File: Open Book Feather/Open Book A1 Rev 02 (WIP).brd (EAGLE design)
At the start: 77.5 x 112.3 mm, 124 parts, among them J1 SJ-43514-SMT, J2 10118193-0001LF, Q1 DMG341, Q2 IRLML0100, SW1 SPDT_SWITCH, U1 AP2112-3.3, U2 MCP73831T-2ACI/OT, U3 ATSAMD51J64-TQFP(10X10), U4 GD25Q16C (or GD25Q32C), U5 74AC165D, U6 GD25Q16C (or GD25Q32C), U7 23K256-I/SN, U8 MAX4466EXK+T, X1 JSTPH, X2 2x5 0.05" SWD

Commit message: correct component values
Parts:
- L1: value 68uH -> 10uH
- R4, R6: value 270 -> 1K
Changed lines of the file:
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@@
 <attribute name="VALUE" x="3.302" y="102.616" size="0.508" layer="28" font="vector" ratio="18" rot="MR90" align="center"/>
 </element>
-<element name="L1" library="microbuilder" package="INDUCTOR_4X4MM_NR401" value="68uH" x="6.35" y="94.742" smashed="yes" rot="MR270">
+<element name="L1" library="microbuilder" package="INDUCTOR_4X4MM_NR401" value="10uH" x="6.35" y="94.742" smashed="yes" rot="MR270">
 <attribute name="NAME" x="6.382" y="97.114" size="0.508" layer="26" font="vector" ratio="18" rot="MR180" align="center"/>
 <attribute name="VALUE" x="5.366" y="94.844" size="0.508" layer="28" font="vector" ratio="18" rot="MR180" align="center"/>
@@
 <attribute name="VALUE" x="18.088" y="111.887" size="0.508" layer="28" font="vector" ratio="18" rot="MR0" align="center"/>
 </element>
-<element name="R4" library="microbuilder" package="0805-NO" value="270" x="32.2834" y="108.5088" smashed="yes" rot="MR180">
+<element name="R4" library="microbuilder" package="0805-NO" value="1K" x="32.2834" y="108.5088" smashed="yes" rot="MR180">
 <attribute name="NAME" x="32.2834" y="107.315" size="0.508" layer="26" font="vector" ratio="18" rot="MR0" align="center"/>
 <attribute name="VALUE" x="32.2834" y="107.2388" size="0.508" layer="28" font="vector" ratio="18" rot="MR180" align="center"/>
@@
 <attribute name="VALUE" x="26.162" y="37.846" size="0.508" layer="28" font="vector" ratio="18" rot="MR0" align="center"/>
 </element>
-<element name="R6" library="microbuilder" package="0805-NO" value="270" x="45.466" y="108.7882" smashed="yes" rot="MR180">
+<element name="R6" library="microbuilder" package="0805-NO" value="1K" x="45.466" y="108.7882" smashed="yes" rot="MR180">
 <attribute name="NAME" x="47.4472" y="108.458" size="0.508" layer="26" font="vector" ratio="18" rot="MR90" align="center"/>
 <attribute name="VALUE" x="47.0662" y="109.9312" size="0.508" layer="28" font="vector" ratio="18" rot="MR180" align="center"/>

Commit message: remove wire stub
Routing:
- net N$65: track 4.96 -> 4.45 mm
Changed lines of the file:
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@@
 <contactref element="R19" pad="2"/>
 <contactref element="R20" pad="1"/>
-<wire x1="65.344" y1="1.524" x2="65.852" y2="1.524" width="0.1524" layer="16"/>
 <wire x1="65.852" y1="1.524" x2="64.676" y2="2.7" width="0.1524" layer="16"/>
 <wire x1="64.676" y1="2.7" x2="64.008" y2="3.368" width="0.1524" layer="16"/>

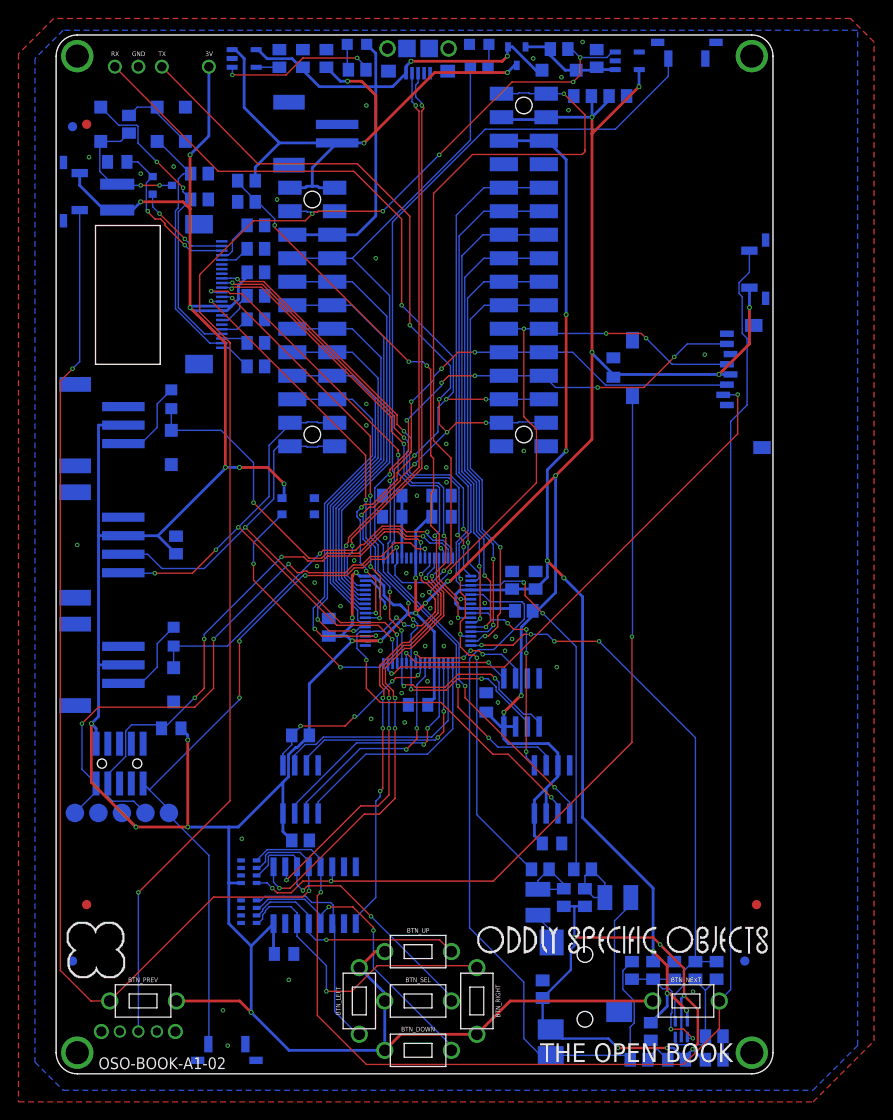
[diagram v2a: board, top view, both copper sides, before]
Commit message: add documentation to front side
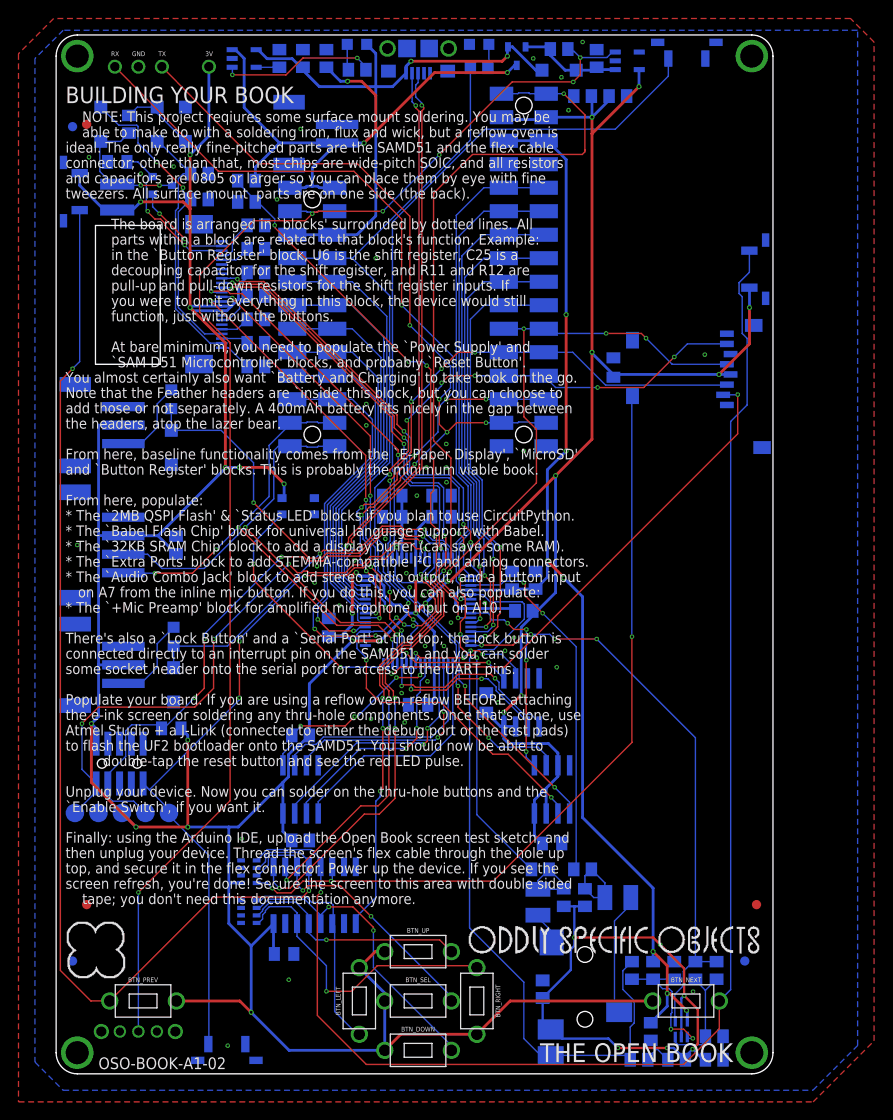
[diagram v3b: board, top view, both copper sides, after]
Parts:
- moved U$48 0.91 mm to (44.3, 14.5)
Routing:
- net GND: vias 49 -> 48
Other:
- board text added: "BATTERY AND CHARGING"
- board text added: "BUILDING YOUR BOOK"
- board text added: "NOTE: This project reqiures some surface mount soldering. You may be able to make do with a soldering iron, flux and wick, but a reflow oven is ideal. The only really fine-pitched parts are the SAMD51 and the flex cable connector; other than that, most chips are wide-pitch SOIC, and all resistors and capacitors are 0805 or larger so you can place them by eye with fine tweezers. All surface mount 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"
- board text removed: "USB, BATTERY AND LOGO:"

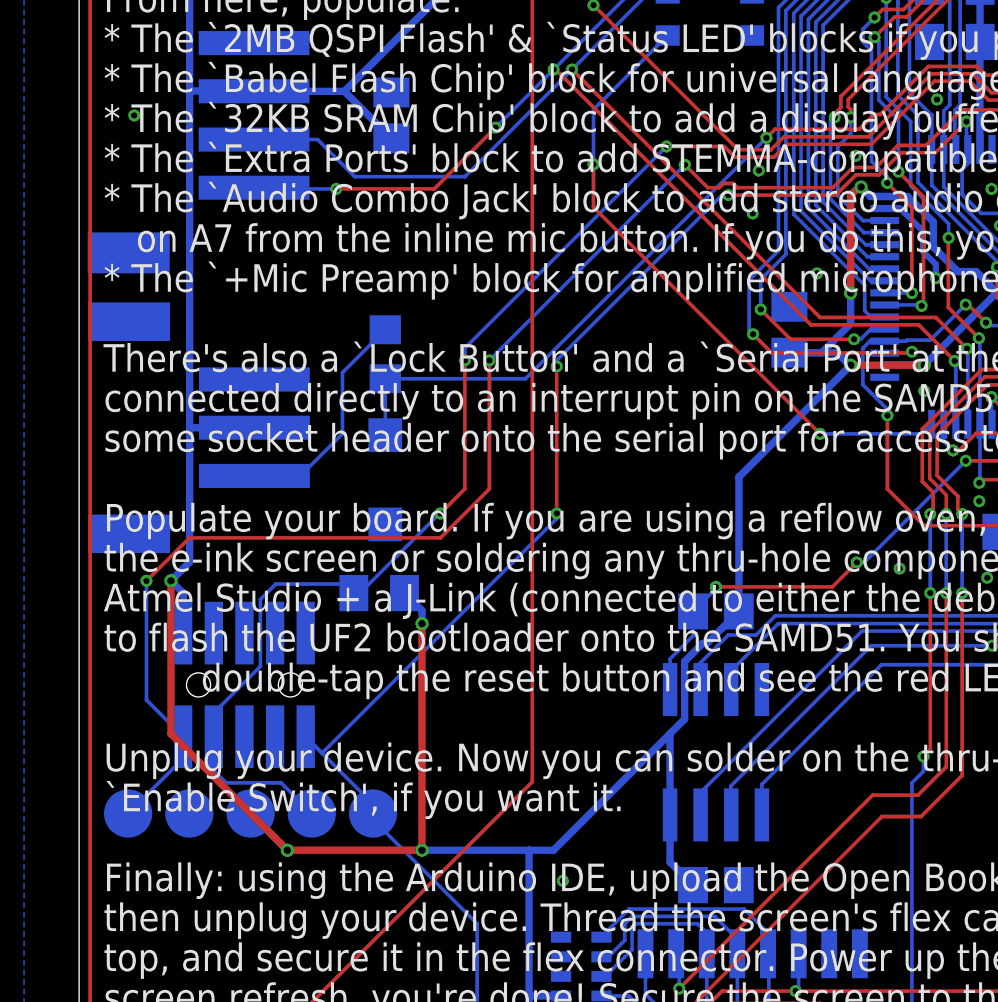
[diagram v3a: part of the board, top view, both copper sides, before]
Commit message: move SWCLK pullup to microcontroller block
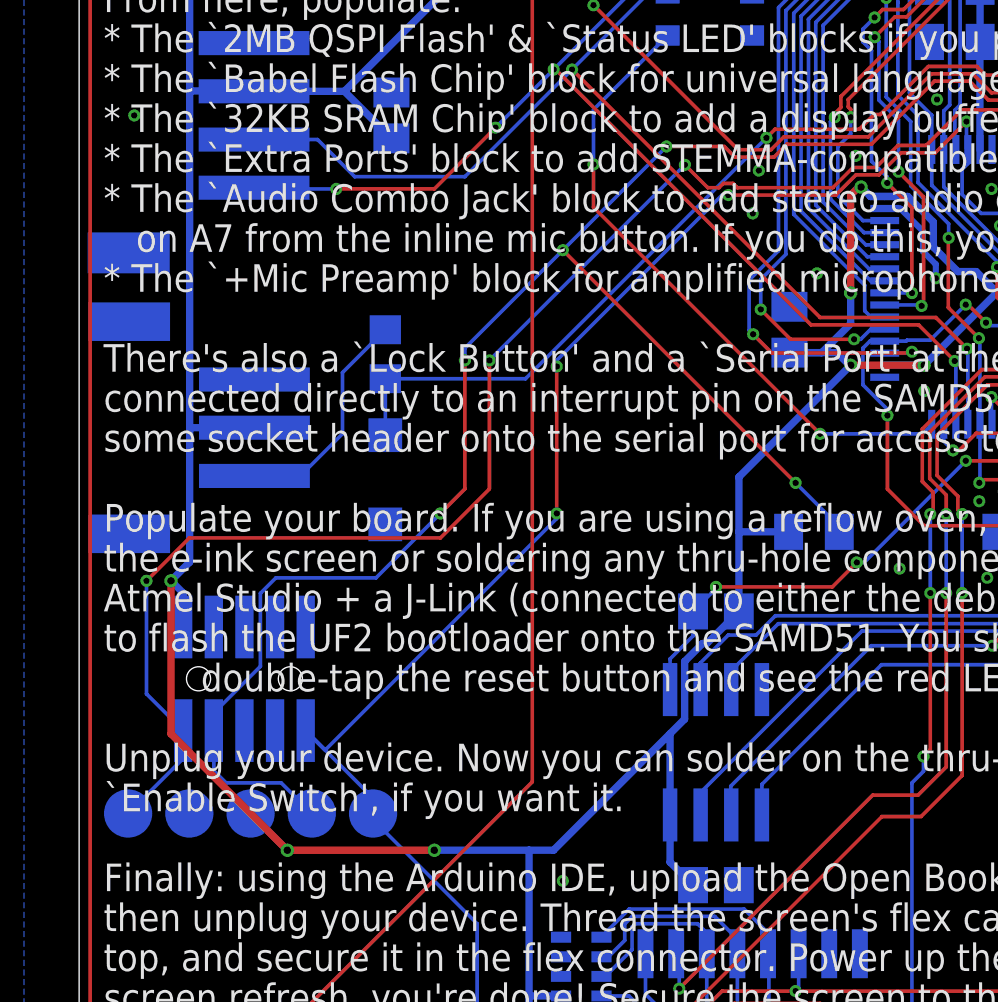
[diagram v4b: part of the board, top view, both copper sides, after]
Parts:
- moved R5 18.2 mm to (30.2, 39.9), turned to 180 degrees
- moved X2 0.25 mm to (6.60, 33.8)
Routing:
- net SWCLK: track 59.8 -> 76.1 mm, vias 4 -> 6
- net +3V3: track 534.1 -> 524.9 mm, vias 27 -> 26
